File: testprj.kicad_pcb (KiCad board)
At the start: 4 copper layers, 98 parts, among them J10 AudioJack3_SwitchTR, J4 Conn_01x40_MountingPin, J7 AudioJack3_SwitchTR, J8 AudioJack3_SwitchTR, J9 AudioJack3_SwitchTR, SW1 SW_Push, SW10 SW_Push, SW11 SW_Push, SW12 SW_Push, SW13 SW_Push, SW14 SW_Push, SW15 SW_Push, SW16 SW_Push, SW17 SW_Push, SW18 SW_Push, SW19 SW_Push, SW2 SW_Push, SW20 SW_Push, SW3 SW_Push, SW4 SW_Push, SW5 SW_Push, SW6 SW_Push, SW7 SW_Push, SW8 SW_Push, SW9 SW_Push, U1 USBLC6-2SC6, U10 USBLC6-2SC6, U11 MCP3208, U12 SN74LVC1G125DBV, U13 74LVC1G32, U2 ST1S10PHR, U3 LM4950TS, U4 74HC595, U5 W25Q128JVE, U6 74HC595, U7 74HC595, U8 74HC595, U9 USBLC6-2SC6, Y2 Crystal_GND24

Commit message: save state
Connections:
- net LCD.B3 renamed /cpu/LCD.B3
- net LCD.B4 renamed /cpu/LCD.B4
- net LCD.B5 renamed /cpu/LCD.B5
- net LCD.B6 renamed /cpu/LCD.B6
- net LCD.B7 renamed /cpu/LCD.B7
- net LCD.CLK renamed /cpu/LCD.CLK
- net LCD.DE renamed /cpu/LCD.DE
- net LCD.G2 renamed /cpu/LCD.G2
- net LCD.G3 renamed /cpu/LCD.G3
- net LCD.G4 renamed /cpu/LCD.G4
- net LCD.G5 renamed /cpu/LCD.G5
- net LCD.G6 renamed /cpu/LCD.G6
- net LCD.G7 renamed /cpu/LCD.G7
- net LCD.HSYNC renamed /cpu/LCD.HSYNC
- net LCD.PWM renamed /cpu/LCD.PWM
- net LCD.R3 renamed /cpu/LCD.R3
- net LCD.R4 renamed /cpu/LCD.R4
- net LCD.R5 renamed /cpu/LCD.R5
- net LCD.R6 renamed /cpu/LCD.R6
- net LCD.R7 renamed /cpu/LCD.R7
- net LCD.VSYNC renamed /cpu/LCD.VSYNC
- U10 pad 5: unconnected-(U10-VBUS-Pad5) -> /control/DVDD_5P0
- U12 pad 5: unconnected-(U12-VCC-Pad5) -> /control/DVDD_3P3
- U13 pad 5: unconnected-(U13-VCC-Pad5) -> /control/DVDD_3P3
- U9 pad 5: unconnected-(U9-VBUS-Pad5) -> /control/DVDD_5P0
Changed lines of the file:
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@@
 			(layers "F.Cu" "F.Mask" "F.Paste")
 			(roundrect_rratio 0.25)
-			(net "unconnected-(U9-VBUS-Pad5)")
+			(net "/control/DVDD_5P0")
 			(pinfunction "VBUS_5")
 			(pintype "passive")
@@
 			(layers "F.Cu" "F.Mask" "F.Paste")
 			(roundrect_rratio 0.25)
-			(net "unconnected-(U12-VCC-Pad5)")
+			(net "/control/DVDD_3P3")
 			(pinfunction "VCC_5")
 			(pintype "power_in")
@@
 			(layers "F.Cu" "F.Mask" "F.Paste")
 			(roundrect_rratio 0.25)
-			(net "unconnected-(U10-VBUS-Pad5)")
+			(net "/control/DVDD_5P0")
 			(pinfunction "VBUS_5")
 			(pintype "passive")
@@
 			(layers "F.Cu" "F.Mask" "F.Paste")
 			(roundrect_rratio 0.25)
-			(net "unconnected-(U13-VCC-Pad5)")
+			(net "/control/DVDD_3P3")
 			(pinfunction "VCC_5")
 			(pintype "power_in")
@@
 			(layers "F.Cu" "F.Mask" "F.Paste")
 			(roundrect_rratio 0.25)
-			(net "LCD.R5")
+			(net "/cpu/LCD.R5")
 			(pinfunction "Pin_5_5")
 			(pintype "passive")
@@
 			(layers "F.Cu" "F.Mask" "F.Paste")
 			(roundrect_rratio 0.25)
-			(net "LCD.R6")
+			(net "/cpu/LCD.R6")
 			(pinfunction "Pin_6_6")
 			(pintype "passive")
@@
 			(layers "F.Cu" "F.Mask" "F.Paste")
 			(roundrect_rratio 0.25)
-			(net "LCD.R7")
+			(net "/cpu/LCD.R7")
 			(pinfunction "Pin_7_7")
 			(pintype "passive")
@@
 			(layers "F.Cu" "F.Mask" "F.Paste")
 			(roundrect_rratio 0.25)
-			(net "LCD.R3")
+			(net "/cpu/LCD.R3")
 			(pinfunction "Pin_8_8")
 			(pintype "passive")
@@
 			(layers "F.Cu" "F.Mask" "F.Paste")
 			(roundrect_rratio 0.25)
-			(net "LCD.R4")
+			(net "/cpu/LCD.R4")
 			(pinfunction "Pin_9_9")
 			(pintype "passive")
@@
 			(layers "F.Cu" "F.Mask" "F.Paste")
 			(roundrect_rratio 0.25)
-			(net "LCD.R5")
+			(net "/cpu/LCD.R5")
 			(pinfunction "Pin_10_10")
 			(pintype "passive")
@@
 			(layers "F.Cu" "F.Mask" "F.Paste")
 			(roundrect_rratio 0.25)
-			(net "LCD.R6")
+			(net "/cpu/LCD.R6")
 			(pinfunction "Pin_11_11")
 			(pintype "passive")
@@
 			(layers "F.Cu" "F.Mask" "F.Paste")
 			(roundrect_rratio 0.25)
-			(net "LCD.R7")
+			(net "/cpu/LCD.R7")
 			(pinfunction "Pin_12_12")
 			(pintype "passive")
@@
 			(layers "F.Cu" "F.Mask" "F.Paste")
 			(roundrect_rratio 0.25)
-			(net "LCD.G6")
+			(net "/cpu/LCD.G6")
 			(pinfunction "Pin_13_13")
 			(pintype "passive")
@@
 			(layers "F.Cu" "F.Mask" "F.Paste")
 			(roundrect_rratio 0.25)
-			(net "LCD.G7")
+			(net "/cpu/LCD.G7")
 			(pinfunction "Pin_14_14")
 			(pintype "passive")
@@
 			(layers "F.Cu" "F.Mask" "F.Paste")
 			(roundrect_rratio 0.25)
-			(net "LCD.G2")
+			(net "/cpu/LCD.G2")
 			(pinfunction "Pin_15_15")
 			(pintype "passive")
@@
 			(layers "F.Cu" "F.Mask" "F.Paste")
 			(roundrect_rratio 0.25)
-			(net "LCD.G3")
+			(net "/cpu/LCD.G3")
 			(pinfunction "Pin_16_16")
 			(pintype "passive")
@@
 			(layers "F.Cu" "F.Mask" "F.Paste")
 			(roundrect_rratio 0.25)
-			(net "LCD.G4")
+			(net "/cpu/LCD.G4")
 			(pinfunction "Pin_17_17")
 			(pintype "passive")
@@
 			(layers "F.Cu" "F.Mask" "F.Paste")
 			(roundrect_rratio 0.25)
-			(net "LCD.G5")
+			(net "/cpu/LCD.G5")
 			(pinfunction "Pin_18_18")
 			(pintype "passive")
@@
 			(layers "F.Cu" "F.Mask" "F.Paste")
 			(roundrect_rratio 0.25)
-			(net "LCD.G6")
+			(net "/cpu/LCD.G6")
 			(pinfunction "Pin_19_19")
 			(pintype "passive")
@@
 			(layers "F.Cu" "F.Mask" "F.Paste")
 			(roundrect_rratio 0.25)
-			(net "LCD.G7")
+			(net "/cpu/LCD.G7")
 			(pinfunction "Pin_20_20")
 			(pintype "passive")
@@
 			(layers "F.Cu" "F.Mask" "F.Paste")
 			(roundrect_rratio 0.25)
-			(net "LCD.B5")
+			(net "/cpu/LCD.B5")
 			(pinfunction "Pin_21_21")
 			(pintype "passive")
@@
 			(layers "F.Cu" "F.Mask" "F.Paste")
 			(roundrect_rratio 0.25)
-			(net "LCD.B6")
+			(net "/cpu/LCD.B6")
 			(pinfunction "Pin_22_22")
 			(pintype "passive")
@@
 			(layers "F.Cu" "F.Mask" "F.Paste")
 			(roundrect_rratio 0.25)
-			(net "LCD.B7")
+			(net "/cpu/LCD.B7")
 			(pinfunction "Pin_23_23")
 			(pintype "passive")
@@
 			(layers "F.Cu" "F.Mask" "F.Paste")
 			(roundrect_rratio 0.25)
-			(net "LCD.B3")
+			(net "/cpu/LCD.B3")
 			(pinfunction "Pin_24_24")
 			(pintype "passive")
@@
 			(layers "F.Cu" "F.Mask" "F.Paste")
 			(roundrect_rratio 0.25)
-			(net "LCD.B4")
+			(net "/cpu/LCD.B4")
 			(pinfunction "Pin_25_25")
 			(pintype "passive")
@@
 			(layers "F.Cu" "F.Mask" "F.Paste")
 			(roundrect_rratio 0.25)
-			(net "LCD.B5")
+			(net "/cpu/LCD.B5")
 			(pinfunction "Pin_26_26")
 			(pintype "passive")
@@
 			(layers "F.Cu" "F.Mask" "F.Paste")
 			(roundrect_rratio 0.25)
-			(net "LCD.B6")
+			(net "/cpu/LCD.B6")
 			(pinfunction "Pin_27_27")
 			(pintype "passive")
@@
 			(layers "F.Cu" "F.Mask" "F.Paste")
 			(roundrect_rratio 0.25)
-			(net "LCD.B7")
+			(net "/cpu/LCD.B7")
 			(pinfunction "Pin_28_28")
 			(pintype "passive")
@@
 			(layers "F.Cu" "F.Mask" "F.Paste")
 			(roundrect_rratio 0.25)
-			(net "LCD.CLK")
+			(net "/cpu/LCD.CLK")
 			(pinfunction "Pin_30_30")
 			(pintype "passive")
@@
 			(layers "F.Cu" "F.Mask" "F.Paste")
 			(roundrect_rratio 0.25)
-			(net "LCD.HSYNC")
+			(net "/cpu/LCD.HSYNC")
 			(pinfunction "Pin_32_32")
 			(pintype "passive")
@@
 			(layers "F.Cu" "F.Mask" "F.Paste")
 			(roundrect_rratio 0.25)
-			(net "LCD.VSYNC")
+			(net "/cpu/LCD.VSYNC")
 			(pinfunction "Pin_33_33")
 			(pintype "passive")
@@
 			(layers "F.Cu" "F.Mask" "F.Paste")
 			(roundrect_rratio 0.25)
-			(net "LCD.DE")
+			(net "/cpu/LCD.DE")
 			(pinfunction "Pin_34_34")
 			(pintype "passive")
@@
 			(layers "F.Cu" "F.Mask" "F.Paste")
 			(roundrect_rratio 0.25)
-			(net "LCD.PWM")
+			(net "/cpu/LCD.PWM")
 			(pinfunction "PD22_52")
 			(pintype "bidirectional")
@@
 			(layers "F.Cu" "F.Mask" "F.Paste")
 			(roundrect_rratio 0.25)
-			(net "LCD.VSYNC")
+			(net "/cpu/LCD.VSYNC")
 			(pinfunction "PD21_53")
 			(pintype "bidirectional")
@@
 			(layers "F.Cu" "F.Mask" "F.Paste")
 			(roundrect_rratio 0.25)
-			(net "LCD.HSYNC")
+			(net "/cpu/LCD.HSYNC")
 			(pinfunction "PD20_54")
 			(pintype "bidirectional")
@@
 			(layers "F.Cu" "F.Mask" "F.Paste")
 			(roundrect_rratio 0.25)
-			(net "LCD.B7")
+			(net "/cpu/LCD.B7")
 			(pinfunction "PD0_55")
 			(pintype "bidirectional")
@@
 			(layers "F.Cu" "F.Mask" "F.Paste")
 			(roundrect_rratio 0.25)
-			(net "LCD.B4")
+			(net "/cpu/LCD.B4")
 			(pinfunction "PD2_57")
 			(pintype "bidirectional")
@@
 			(layers "F.Cu" "F.Mask" "F.Paste")
 			(roundrect_rratio 0.25)
-			(net "LCD.B5")
+			(net "/cpu/LCD.B5")
 			(pinfunction "PD3_58")
 			(pintype "bidirectional")
@@
 			(layers "F.Cu" "F.Mask" "F.Paste")
 			(roundrect_rratio 0.25)
-			(net "LCD.B6")
+			(net "/cpu/LCD.B6")
 			(pinfunction "PD4_59")
 			(pintype "bidirectional")
@@
 			(layers "F.Cu" "F.Mask" "F.Paste")
 			(roundrect_rratio 0.25)
-			(net "LCD.B7")
+			(net "/cpu/LCD.B7")
 			(pinfunction "PD5_60")
 			(pintype "bidirectional")
@@
 			(layers "F.Cu" "F.Mask" "F.Paste")
 			(roundrect_rratio 0.25)
-			(net "LCD.G2")
+			(net "/cpu/LCD.G2")
 			(pinfunction "PD6_61")
 			(pintype "bidirectional")
@@
 			(layers "F.Cu" "F.Mask" "F.Paste")
 			(roundrect_rratio 0.25)
-			(net "LCD.G3")
+			(net "/cpu/LCD.G3")
 			(pinfunction "PD7_62")
 			(pintype "bidirectional")
@@
 			(layers "F.Cu" "F.Mask" "F.Paste")
 			(roundrect_rratio 0.25)
-			(net "LCD.G4")
+			(net "/cpu/LCD.G4")
 			(pinfunction "PD8_63")
 			(pintype "bidirectional")
@@
 			(layers "F.Cu" "F.Mask" "F.Paste")
 			(roundrect_rratio 0.25)
-			(net "LCD.G5")
+			(net "/cpu/LCD.G5")
 			(pinfunction "PD9_64")
 			(pintype "bidirectional")
@@
 			(layers "F.Cu" "F.Mask" "F.Paste")
 			(roundrect_rratio 0.25)
-			(net "LCD.G6")
+			(net "/cpu/LCD.G6")
 			(pinfunction "PD10_67")
 			(pintype "bidirectional")
@@
 			(layers "F.Cu" "F.Mask" "F.Paste")
 			(roundrect_rratio 0.25)
-			(net "LCD.G7")
+			(net "/cpu/LCD.G7")
 			(pinfunction "PD11_68")
 			(pintype "bidirectional")
@@
 			(layers "F.Cu" "F.Mask" "F.Paste")
 			(roundrect_rratio 0.25)
-			(net "LCD.R3")
+			(net "/cpu/LCD.R3")
 			(pinfunction "PD13_69")
 			(pintype "bidirectional")
@@
 			(layers "F.Cu" "F.Mask" "F.Paste")
 			(roundrect_rratio 0.25)
-			(net "LCD.R4")
+			(net "/cpu/LCD.R4")
 			(pinfunction "PD14_71")
 			(pintype "bidirectional")
@@
 			(layers "F.Cu" "F.Mask" "F.Paste")
 			(roundrect_rratio 0.25)
-			(net "LCD.R5")
+			(net "/cpu/LCD.R5")
 			(pinfunction "PD15_72")
 			(pintype "bidirectional")
@@
 			(layers "F.Cu" "F.Mask" "F.Paste")
 			(roundrect_rratio 0.25)
-			(net "LCD.R6")
+			(net "/cpu/LCD.R6")
 			(pinfunction "PD16_73")
 			(pintype "bidirectional")
@@
 			(layers "F.Cu" "F.Mask" "F.Paste")
 			(roundrect_rratio 0.25)
-			(net "LCD.R7")
+			(net "/cpu/LCD.R7")
 			(pinfunction "PD17_74")
 			(pintype "bidirectional")
@@
 			(layers "F.Cu" "F.Mask" "F.Paste")
 			(roundrect_rratio 0.25)
-			(net "LCD.CLK")
+			(net "/cpu/LCD.CLK")
 			(pinfunction "PD18_75")
 			(pintype "bidirectional")
@@
 			(layers "F.Cu" "F.Mask" "F.Paste")
 			(roundrect_rratio 0.25)
-			(net "LCD.DE")
+			(net "/cpu/LCD.DE")
 			(pinfunction "PD19_76")
 			(pintype "bidirectional")

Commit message: save state
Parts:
- added U14: 74LVC1G32, Package_TO_SOT_SMD:SOT-23-5, F.Cu at (277.6, 133.6)
- moved C3 165.0 mm to (269.4, 106.2)
- moved C4 165.0 mm to (269.4, 114.3)
- moved DD1 165.0 mm to (266.1, 127.4)
- moved U12 165.0 mm to (271.2, 144.9)
- moved U13 165.0 mm to (269.7, 155.9)
- moved R10 165.0 mm to (293.1, 125.2)
- moved R11 165.0 mm to (293.1, 128.2)
- moved R12 165.0 mm to (293.1, 131.1)
- moved R13 165.0 mm to (293.1, 134.1)
- moved U10 165.0 mm to (298.0, 130.8)
- moved U3 165.0 mm to (250.3, 129.9)
- moved U4 165.0 mm to (281.5, 105.4)
- moved U6 165.0 mm to (281.5, 112.0)
- moved U7 165.0 mm to (281.5, 118.6)
- moved U8 165.0 mm to (281.5, 125.2)
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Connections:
- U13 pad 2: unconnected-(U13-Pad2) -> Net-(U4-RCLK)
- U13 pad 4: unconnected-(U13-Pad4) -> Net-(U4-SER)
- U4 pad 10: unconnected-(U4-~{SRCLR}-Pad10) -> /control/DVDD_3P3
- U4 pad 14: unconnected-(U4-SER-Pad14) -> Net-(U4-SER)
- U4 pad 16: unconnected-(U4-VCC-Pad16) -> /control/DVDD_3P3
- U6 pad 10: unconnected-(U6-~{SRCLR}-Pad10) -> /control/DVDD_3P3
- U6 pad 13: unconnected-(U6-~{OE}-Pad13) -> /control/DVDD_3P3
- U6 pad 16: unconnected-(U6-VCC-Pad16) -> /control/DVDD_3P3
- U6 pad 9: unconnected-(U6-QH'-Pad9) -> Net-(U6-QH')
- U7 pad 10: unconnected-(U7-~{SRCLR}-Pad10) -> /control/DVDD_3P3
- U7 pad 14: unconnected-(U7-SER-Pad14) -> Net-(U6-QH')
- U7 pad 16: unconnected-(U7-VCC-Pad16) -> /control/DVDD_3P3
- U7 pad 9: unconnected-(U7-QH'-Pad9) -> Net-(U7-QH')
- U8 pad 10: unconnected-(U8-~{SRCLR}-Pad10) -> /control/DVDD_3P3
- U8 pad 14: unconnected-(U8-SER-Pad14) -> Net-(U7-QH')
- U8 pad 16: unconnected-(U8-VCC-Pad16) -> /control/DVDD_3P3
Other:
- board outline added: 286.5 x 81.5 mm

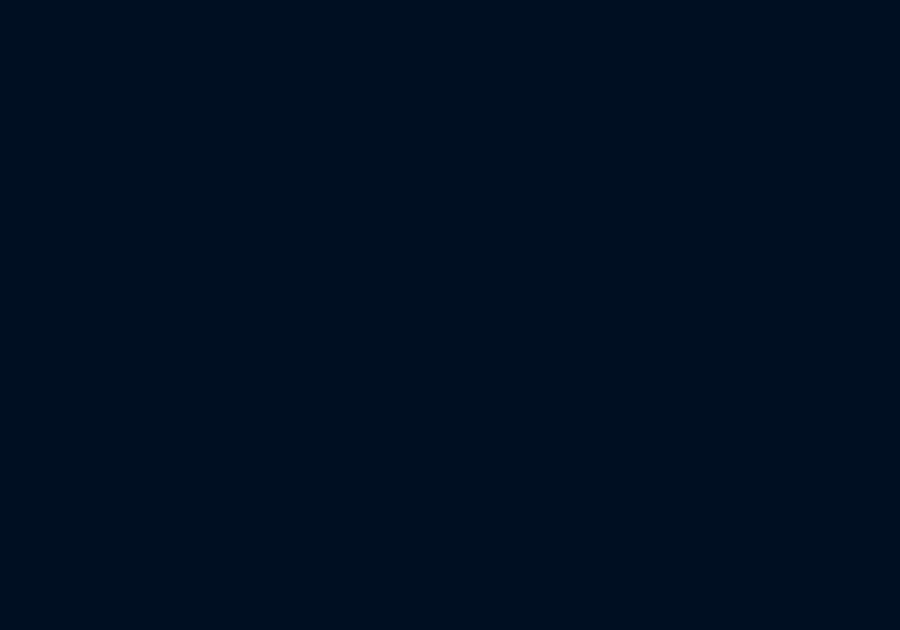
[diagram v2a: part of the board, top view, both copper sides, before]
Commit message: Add ES9822QPRO
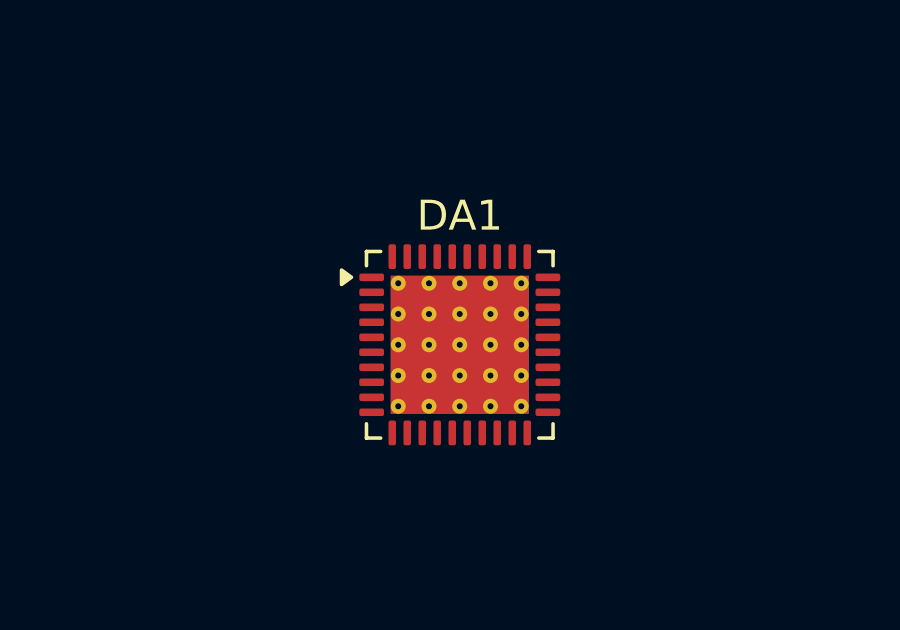
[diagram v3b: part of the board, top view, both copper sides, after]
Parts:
- added DA1: ES9822PRO, Package_DFN_QFN:QFN-40-1EP_6x6mm_P0.5mm_EP4.6x4.6mm_ThermalVias, F.Cu at (122.5, 147.6)

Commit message: Add ULN2003
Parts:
- added U15: ULN2002A, Package_SO:TSSOP-16_4.4x5mm_P0.65mm, F.Cu at (300.4, 115.2)
- added U16: ULN2002A, Package_SO:TSSOP-16_4.4x5mm_P0.65mm, F.Cu at (300.5, 107.5)
- added U17: ULN2002A, Package_SO:TSSOP-16_4.4x5mm_P0.65mm, F.Cu at (300.5, 100.0)
- added U18: ULN2002A, Package_SO:TSSOP-16_4.4x5mm_P0.65mm, F.Cu at (300.0, 93.0)
- moved U4 14.1 mm to (289.0, 93.5), turned to 180 degrees
- moved U6 13.8 mm to (288.9, 100.3), turned to 180 degrees
- moved U7 13.1 mm to (288.9, 107.8), turned to 180 degrees
- moved U8 12.3 mm to (288.9, 115.3), turned to 180 degrees
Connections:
- U4 pad 1: unconnected-(U4-QB-Pad1) -> Net-(U18-I7)
- U4 pad 2: unconnected-(U4-QC-Pad2) -> Net-(U18-I6)
- U4 pad 3: unconnected-(U4-QD-Pad3) -> Net-(U18-I5)
- U4 pad 4: unconnected-(U4-QE-Pad4) -> Net-(U18-I4)
- U4 pad 5: unconnected-(U4-QF-Pad5) -> Net-(U18-I3)
- U4 pad 6: unconnected-(U4-QG-Pad6) -> Net-(U18-I2)
- U4 pad 7: unconnected-(U4-QH-Pad7) -> Net-(U18-I1)
- U6 pad 1: unconnected-(U6-QB-Pad1) -> Net-(U17-I7)
- U6 pad 2: unconnected-(U6-QC-Pad2) -> Net-(U17-I6)
- U6 pad 3: unconnected-(U6-QD-Pad3) -> Net-(U17-I5)
- U6 pad 4: unconnected-(U6-QE-Pad4) -> Net-(U17-I4)
- U6 pad 5: unconnected-(U6-QF-Pad5) -> Net-(U17-I3)
- U6 pad 6: unconnected-(U6-QG-Pad6) -> Net-(U17-I2)
- U6 pad 7: unconnected-(U6-QH-Pad7) -> Net-(U17-I1)
- U7 pad 1: unconnected-(U7-QB-Pad1) -> Net-(U16-I7)
- U7 pad 2: unconnected-(U7-QC-Pad2) -> Net-(U16-I6)
- U7 pad 3: unconnected-(U7-QD-Pad3) -> Net-(U16-I5)
- U7 pad 4: unconnected-(U7-QE-Pad4) -> Net-(U16-I4)
- U7 pad 5: unconnected-(U7-QF-Pad5) -> Net-(U16-I3)
- U7 pad 6: unconnected-(U7-QG-Pad6) -> Net-(U16-I2)
- U7 pad 7: unconnected-(U7-QH-Pad7) -> Net-(U16-I1)
- U8 pad 1: unconnected-(U8-QB-Pad1) -> Net-(U15-I7)
- U8 pad 2: unconnected-(U8-QC-Pad2) -> Net-(U15-I6)
- U8 pad 3: unconnected-(U8-QD-Pad3) -> Net-(U15-I5)
- U8 pad 4: unconnected-(U8-QE-Pad4) -> Net-(U15-I4)
- U8 pad 5: unconnected-(U8-QF-Pad5) -> Net-(U15-I3)
- U8 pad 6: unconnected-(U8-QG-Pad6) -> Net-(U15-I2)
- U8 pad 7: unconnected-(U8-QH-Pad7) -> Net-(U15-I1)

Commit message: Использование power symbols
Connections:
- net /control/DVDD_3P3 renamed DVDD1_3P3
- net /control/DVDD_5P0 renamed DVDD1_5P0
- C23 pad 2: /cpu/RFDND -> RFGND
- C24 pad 2: /cpu/RFDND -> RFGND
- U3 pad 8: unconnected-(U3A-BYP-Pad8) -> RFGND
- Y2 pad 2: /cpu/RFDND -> RFGND
- Y2 pad 4: /cpu/RFDND -> RFGND
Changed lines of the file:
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@@
 			(layers "F.Cu" "F.Mask" "F.Paste")
 			(roundrect_rratio 0.25)
-			(net "/control/DVDD_3P3")
+			(net "DVDD1_3P3")
 			(pinfunction "~{SRCLR}_10")
 			(pintype "input")
@@
 			(layers "F.Cu" "F.Mask" "F.Paste")
 			(roundrect_rratio 0.25)
-			(net "/control/DVDD_3P3")
+			(net "DVDD1_3P3")
 			(pinfunction "VCC_16")
 			(pintype "power_in")
@@
 			(layers "F.Cu" "F.Mask" "F.Paste")
 			(roundrect_rratio 0.25)
-			(net "/control/DVDD_3P3")
+			(net "DVDD1_3P3")
 			(pinfunction "~{SRCLR}_10")
 			(pintype "input")
@@
 			(layers "F.Cu" "F.Mask" "F.Paste")
 			(roundrect_rratio 0.25)
-			(net "/control/DVDD_3P3")
+			(net "DVDD1_3P3")
 			(pinfunction "VCC_16")
 			(pintype "power_in")
@@
 			(layers "F.Cu" "F.Mask" "F.Paste")
 			(roundrect_rratio 0.25)
-			(net "/control/DVDD_5P0")
+			(net "DVDD1_5P0")
 			(pinfunction "VBUS_5")
 			(pintype "passive")
@@
 			(layers "F.Cu" "F.Mask" "F.Paste")
 			(roundrect_rratio 0.212766)
-			(net "/cpu/RFDND")
+			(net "RFGND")
 			(pintype "passive")
 		)
@@
 			(layers "F.Cu" "F.Mask" "F.Paste")
 			(roundrect_rratio 0.25)
-			(net "/control/DVDD_3P3")
+			(net "DVDD1_3P3")
 			(pinfunction "~{SRCLR}_10")
 			(pintype "input")
@@
 			(layers "F.Cu" "F.Mask" "F.Paste")
 			(roundrect_rratio 0.25)
-			(net "/control/DVDD_3P3")
+			(net "DVDD1_3P3")
 			(pinfunction "VCC_16")
 			(pintype "power_in")
@@
 			(layers "F.Cu" "F.Mask" "F.Paste")
 			(roundrect_rratio 0.25)
-			(net "/control/DVDD_3P3")
+			(net "DVDD1_3P3")
 			(pinfunction "VCC_5")
 			(pintype "power_in")
@@
 			(layers "F.Cu" "F.Mask" "F.Paste")
 			(roundrect_rratio 0.25)
-			(net "/control/DVDD_5P0")
+			(net "DVDD1_5P0")
 			(pinfunction "VBUS_5")
 			(pintype "passive")
@@
 			(layers "F.Cu" "F.Mask" "F.Paste")
 			(roundrect_rratio 0.25)
-			(net "unconnected-(U3A-BYP-Pad8)")
+			(net "RFGND")
 			(pinfunction "BYP_8")
 			(pintype "passive")
@@
 			(layers "F.Cu" "F.Mask" "F.Paste")
 			(roundrect_rratio 0.25)
-			(net "/control/DVDD_3P3")
+			(net "DVDD1_3P3")
 			(pinfunction "~{SRCLR}_10")
 			(pintype "input")
@@
 			(layers "F.Cu" "F.Mask" "F.Paste")
 			(roundrect_rratio 0.25)
-			(net "/control/DVDD_3P3")
+			(net "DVDD1_3P3")
 			(pinfunction "~{OE}_13")
 			(pintype "input")
@@
 			(layers "F.Cu" "F.Mask" "F.Paste")
 			(roundrect_rratio 0.25)
-			(net "/control/DVDD_3P3")
+			(net "DVDD1_3P3")
 			(pinfunction "VCC_16")
 			(pintype "power_in")
@@
 			(layers "F.Cu" "F.Mask" "F.Paste")
 			(roundrect_rratio 0.147059)
-			(net "/cpu/RFDND")
+			(net "RFGND")
 			(pinfunction "G_2")
 			(pintype "passive")
@@
 			(layers "F.Cu" "F.Mask" "F.Paste")
 			(roundrect_rratio 0.147059)
-			(net "/cpu/RFDND")
+			(net "RFGND")
 			(pinfunction "G_4")
 			(pintype "passive")
@@
 			(layers "F.Cu" "F.Mask" "F.Paste")
 			(roundrect_rratio 0.25)
-			(net "/control/DVDD_3P3")
+			(net "DVDD1_3P3")
 			(pinfunction "VCC_5")
 			(pintype "power_in")
@@
 			(layers "F.Cu" "F.Mask" "F.Paste")
 			(roundrect_rratio 0.25)
-			(net "/control/DVDD_3P3")
+			(net "DVDD1_3P3")
 			(pinfunction "VCC_5")
 			(pintype "power_in")
@@
 			(layers "F.Cu" "F.Mask" "F.Paste")
 			(roundrect_rratio 0.212766)
-			(net "/cpu/RFDND")
+			(net "RFGND")
 			(pintype "passive")
 		)
